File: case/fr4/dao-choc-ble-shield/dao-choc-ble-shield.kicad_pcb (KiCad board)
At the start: 2 copper layers, 24 x 60.6 mm, 5 parts

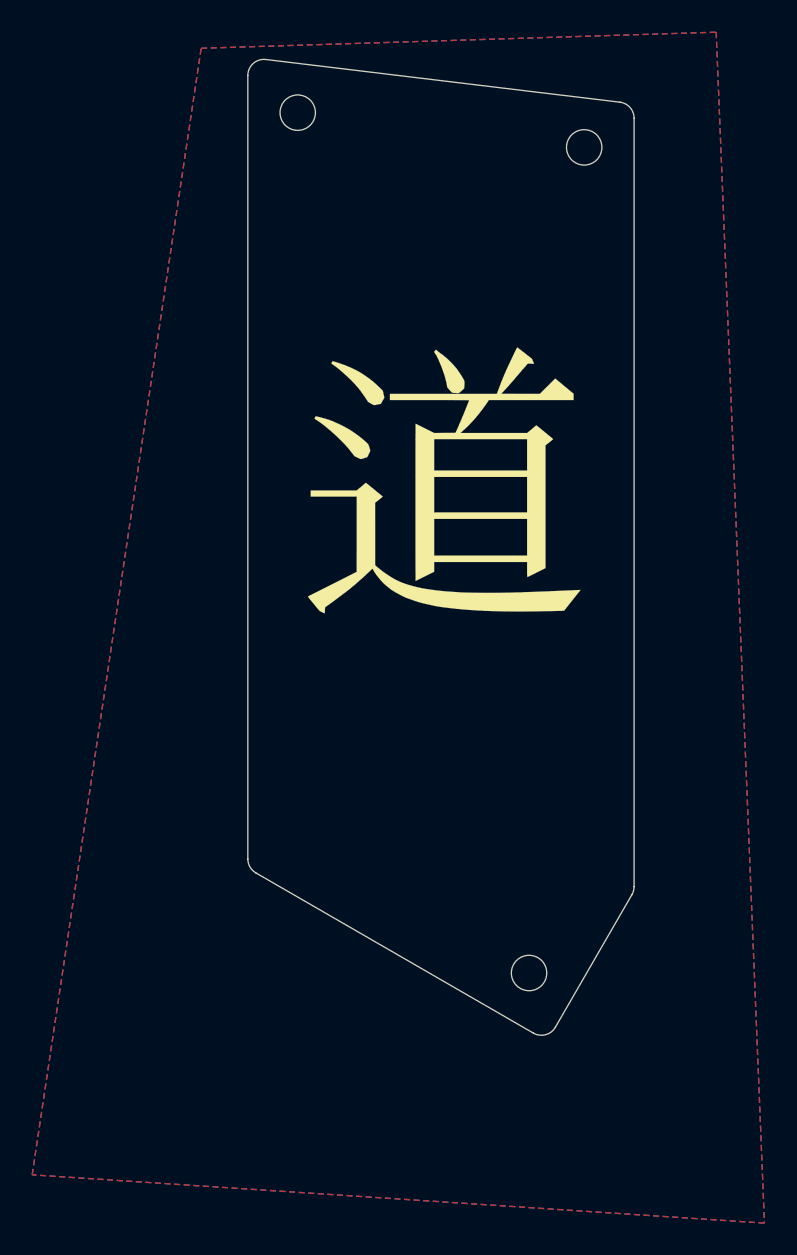
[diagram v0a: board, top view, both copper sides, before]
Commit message: feat: added 42key variant and BOM
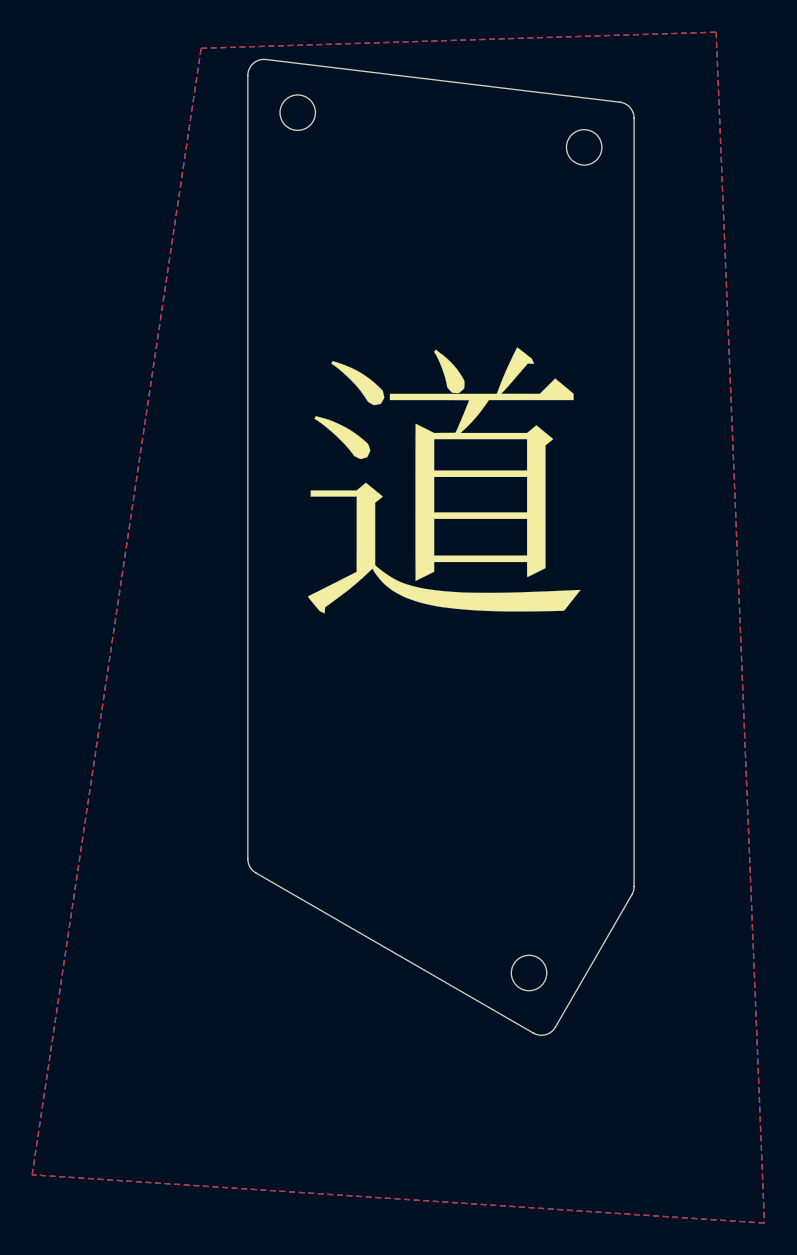
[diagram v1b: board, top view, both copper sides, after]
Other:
- net class Default removed
